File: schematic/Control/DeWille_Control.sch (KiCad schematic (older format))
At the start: 8 parts

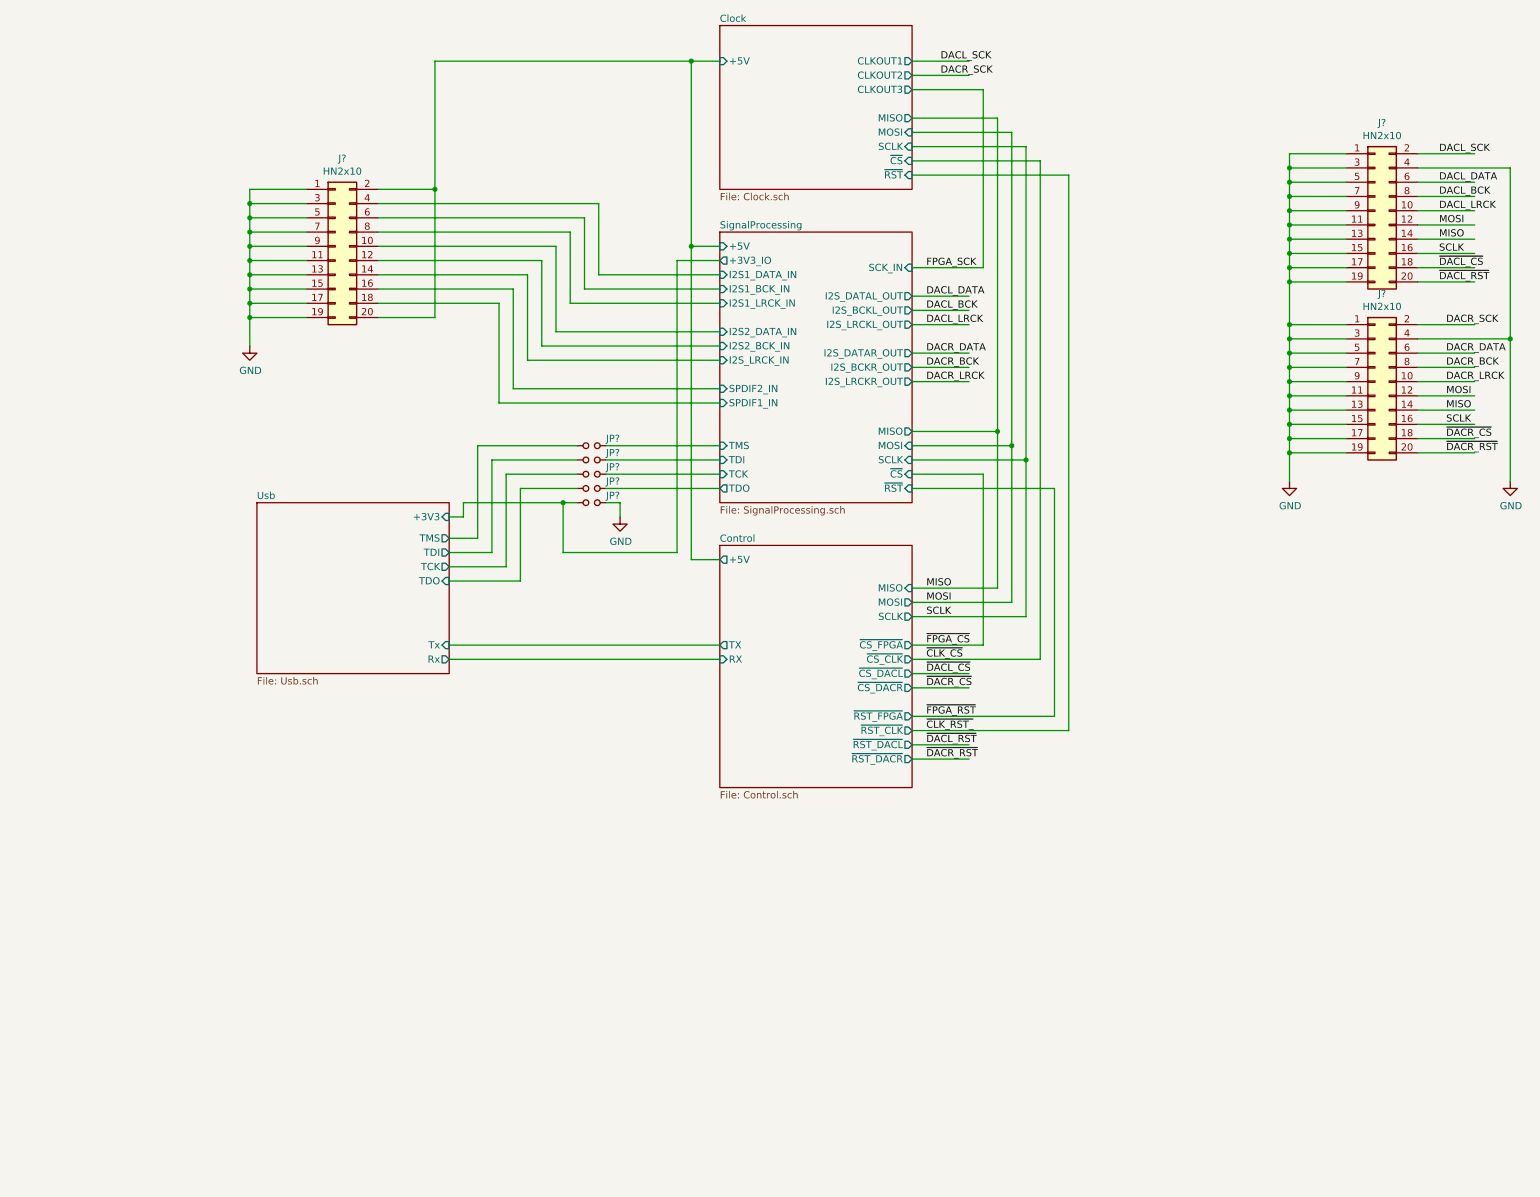
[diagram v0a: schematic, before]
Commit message: Provision for SPI Slave FPGA bitstream download. Switch RAM from x16 to x8 one.
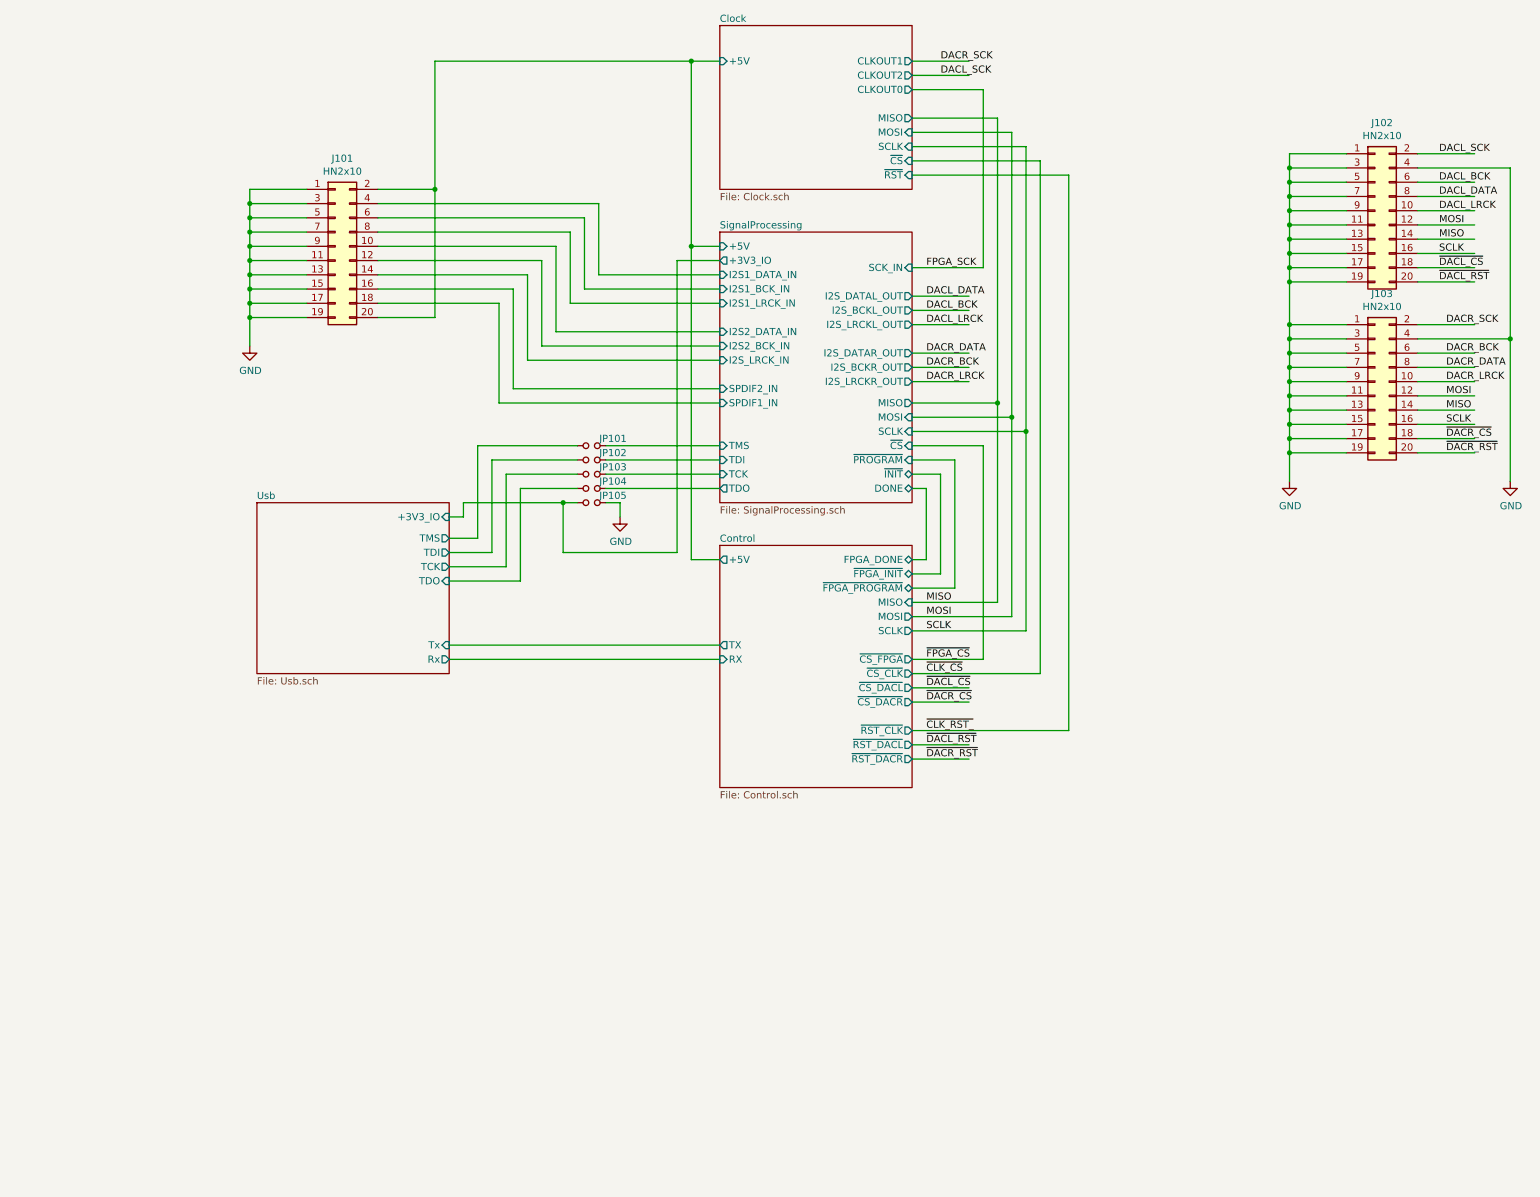
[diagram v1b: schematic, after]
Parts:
- JP101, JP102, JP103, JP104, JP105: renamed from JP?; footprint (none) -> Connector_PinHeader_2.54mm:PinHeader_1x02_P2.54mm_Vertical
- gave numbers to parts that had none: 3
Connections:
- net labels removed: ~FPGA_RST~
- wire segments 186 -> 192

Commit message: Interim commit
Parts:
- added D101: Green, LED_SMD:LED_0805_2012Metric, symbol Device:LED
- added D102, D103, D104, D105: Red, LED_SMD:LED_0805_2012Metric, symbol Device:LED
- added H101, H102, H103, H104: MountingHole, MountingHole:MountingHole_3.2mm_M3_Pad, symbol Mechanical:MountingHole
- added R101, R102, R103, R104, R105: 470, Resistor_SMD:R_0603_1608Metric, symbol Device:R
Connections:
- net labels added: RX, TX
- wire segments 192 -> 225

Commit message: Routing complete
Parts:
- removed JP105: (no value), Connector_PinHeader_2.54mm:PinHeader_1x02_P2.54mm_Vertical, symbol Device:Jumper_NO_Small
- added D?: SM6T6V8CA, Diode_SMD:D_SMB, symbol Diode:1.5KExxCA
- added F?: PFMF.050.2, Fuse:Fuse_1812_4532Metric, symbol Device:Polyfuse
- JP101, JP102, JP103, JP104: footprint Connector_PinHeader_2.54mm:PinHeader_1x02_P2.54mm_Vertical -> Jumper:SolderJumper-2_P1.3mm_Bridged_RoundedPad1.0x1.5mm
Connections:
- wire segments 225 -> 227
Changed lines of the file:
@@
 F18 "LED1" O L 6000 7200 50
 F19 "LED2" O L 6000 7300 50
+F20 "~RST_FPGA~" O R 7350 7400 50
 $EndSheet
 Wire Wire Line
@@
 F4 "MISO" O R 7350 4700 50
 F5 "SCLK" I R 7350 4900 50
-F6 "~CS~" I R 7350 5100 50
+F6 "~FPGA_CS~" I R 7350 5100 50
 F7 "I2S_LRCKL_OUT" O R 7350 4200 50
 F8 "I2S_BCKL_OUT" O R 7350 4100 50
@@
 F17 "I2S2_BCK_IN" I L 6000 4400 50
 F18 "I2S2_LRCK_IN" I L 6000 4500 50
-F19 "SPDIF1_IN" I L 6000 4800 50
-F20 "SPDIF2_IN" I L 6000 4700 50
+F19 "SPDIF1_IN" I L 6000 4700 50
+F20 "SPDIF2_IN" I L 6000 4800 50
 F21 "+5V" I L 6000 3700 50
 F22 "TMS" I L 6000 5100 50
@@
 F 0 "JP101" H 5250 5150 50  0000 C CNN
 F 1 " " H 5100 5194 50  0000 C CNN
-F 2 "Connector_PinHeader_2.54mm:PinHeader_1x02_P2.54mm_Vertical" H 5100 5100 50  0001 C CNN
+F 2 "Jumper:SolderJumper-2_P1.3mm_Bridged_RoundedPad1.0x1.5mm" H 5100 5100 50  0001 C CNN
 F 3 "~" H 5100 5100 50  0001 C CNN
 	1    5100 5100
@@
 F 0 "JP102" H 5250 5250 50  0000 C CNN
 F 1 " " H 5100 5294 50  0000 C CNN
-F 2 "Connector_PinHeader_2.54mm:PinHeader_1x02_P2.54mm_Vertical" H 5100 5200 50  0001 C CNN
+F 2 "Jumper:SolderJumper-2_P1.3mm_Bridged_RoundedPad1.0x1.5mm" H 5100 5200 50  0001 C CNN
 F 3 "~" H 5100 5200 50  0001 C CNN
 	1    5100 5200
@@
 F 0 "JP103" H 5250 5350 50  0000 C CNN
 F 1 " " H 5100 5394 50  0000 C CNN
-F 2 "Connector_PinHeader_2.54mm:PinHeader_1x02_P2.54mm_Vertical" H 5100 5300 50  0001 C CNN
+F 2 "Jumper:SolderJumper-2_P1.3mm_Bridged_RoundedPad1.0x1.5mm" H 5100 5300 50  0001 C CNN
 F 3 "~" H 5100 5300 50  0001 C CNN
 	1    5100 5300
@@
 F 0 "JP104" H 5250 5450 50  0000 C CNN
 F 1 " " H 5100 5494 50  0000 C CNN
-F 2 "Connector_PinHeader_2.54mm:PinHeader_1x02_P2.54mm_Vertical" H 5100 5400 50  0001 C CNN
+F 2 "Jumper:SolderJumper-2_P1.3mm_Bridged_RoundedPad1.0x1.5mm" H 5100 5400 50  0001 C CNN
 F 3 "~" H 5100 5400 50  0001 C CNN
 	1    5100 5400
@@
 Wire Wire Line
 	4600 6050 4100 6050
-$Comp
-L Device:Jumper_NO_Small JP105
-U 1 1 5E2A0271
-P 5100 5500
-F 0 "JP105" H 5250 5550 50  0000 C CNN
-F 1 " " H 5100 5594 50  0000 C CNN
-F 2 "Connector_PinHeader_2.54mm:PinHeader_1x02_P2.54mm_Vertical" H 5100 5500 50  0001 C CNN
-F 3 "~" H 5100 5500 50  0001 C CNN
-	1    5100 5500
-	1    0    0    -1
-$EndComp
 Wire Wire Line
 	4100 5600 4200 5600
@@
 Wire Wire Line
 	4200 5500 4800 5500
-$Comp
-L power:GND #PWR?
-U 1 1 5E2A6414
-P 5300 5600
-AR Path="/5DD2C0D9/5E2A6414" Ref="#PWR?"  Part="1"
-AR Path="/5E2A6414" Ref="#PWR0102"  Part="1"
-F 0 "#PWR0102" H 5300 5350 50  0001 C CNN
-F 1 "GND" H 5305 5427 50  0000 C CNN
-F 2 "" H 5300 5600 50  0001 C CNN
-F 3 "" H 5300 5600 50  0001 C CNN
-	1    5300 5600
-	1    0    0    -1
-$EndComp
-Wire Wire Line
-	5200 5500 5300 5500
-Wire Wire Line
-	5300 5500 5300 5600
 Wire Wire Line
 	3100 4100 2700 4100
@@
 Wire Wire Line
 	4800 5900 4800 5500
-Connection ~ 4800 5500
-Wire Wire Line
-	4800 5500 5000 5500
 Wire Wire Line
 	8250 3100 8250 6700
@@
 	2900 2400 2900 3300
 Wire Wire Line
-	2900 2400 5800 2400
+	2900 2400 3300 2400
 Connection ~ 2900 3300
 Wire Wire Line
@@
 Wire Wire Line
 	5250 3900 6000 3900
+Wire Wire Line
+	7350 7400 8350 7400
+Wire Wire Line
+	8350 7400 8350 5000
+Wire Wire Line
+	8350 5000 7350 5000
+$Comp
+L Device:Polyfuse F?
+U 1 1 5E641952
+P 3450 2400
+F 0 "F?" V 3225 2400 50  0000 C CNN
+F 1 "PFMF.050.2" V 3316 2400 50  0000 C CNN
+F 2 "Fuse:Fuse_1812_4532Metric" H 3500 2200 50  0001 L CNN
+F 3 "~" H 3450 2400 50  0001 C CNN
+	1    3450 2400
+	0    1    1    0
+$EndComp
+$Comp
+L power:GND #PWR?
+U 1 1 5E644AF9
+P 3850 2700
+AR Path="/5DD2C0D9/5E644AF9" Ref="#PWR?"  Part="1"
+AR Path="/5E644AF9" Ref="#PWR?"  Part="1"
+F 0 "#PWR?" H 3850 2450 50  0001 C CNN
+F 1 "GND" H 3855 2527 50  0000 C CNN
+F 2 "" H 3850 2700 50  0001 C CNN
+F 3 "" H 3850 2700 50  0001 C CNN
+	1    3850 2700
+	1    0    0    -1
+$EndComp
+Wire Wire Line
+	3600 2400 3850 2400
+$Comp
+L Diode:1.5KExxCA D?
+U 1 1 5E656D9F
+P 3850 2550
+F 0 "D?" V 3804 2629 50  0000 L CNN
+F 1 "SM6T6V8CA" V 3895 2629 50  0000 L CNN
+F 2 "Diode_SMD:D_SMB" H 3850 2350 50  0001 C CNN
+F 3 "https://www.vishay.com/docs/88301/15ke.pdf" H 3850 2550 50  0001 C CNN
+	1    3850 2550
+	0    1    1    0
+$EndComp
+Connection ~ 3850 2400
+Wire Wire Line
+	3850 2400 5800 2400
 $EndSCHEMATC

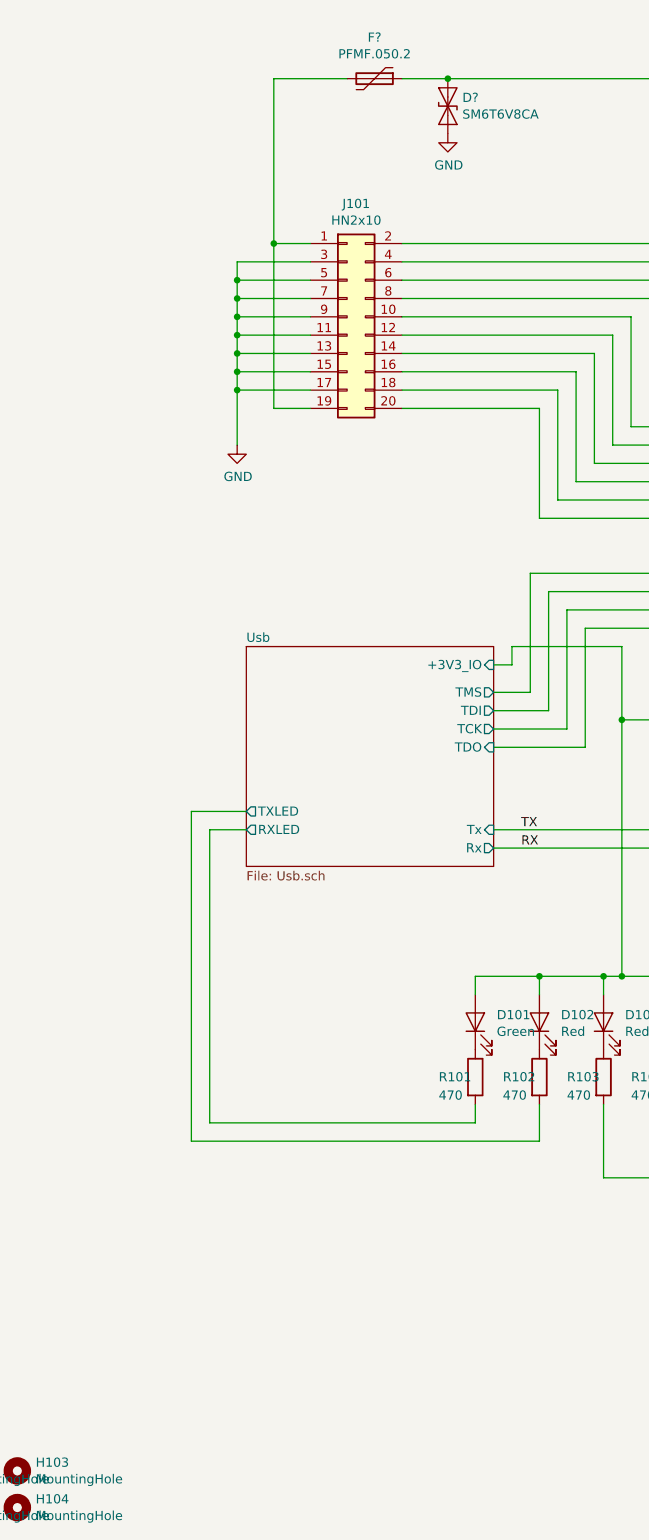
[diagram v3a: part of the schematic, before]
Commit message: Add source termination resistors to I2S output lines. Arrange top silk information.
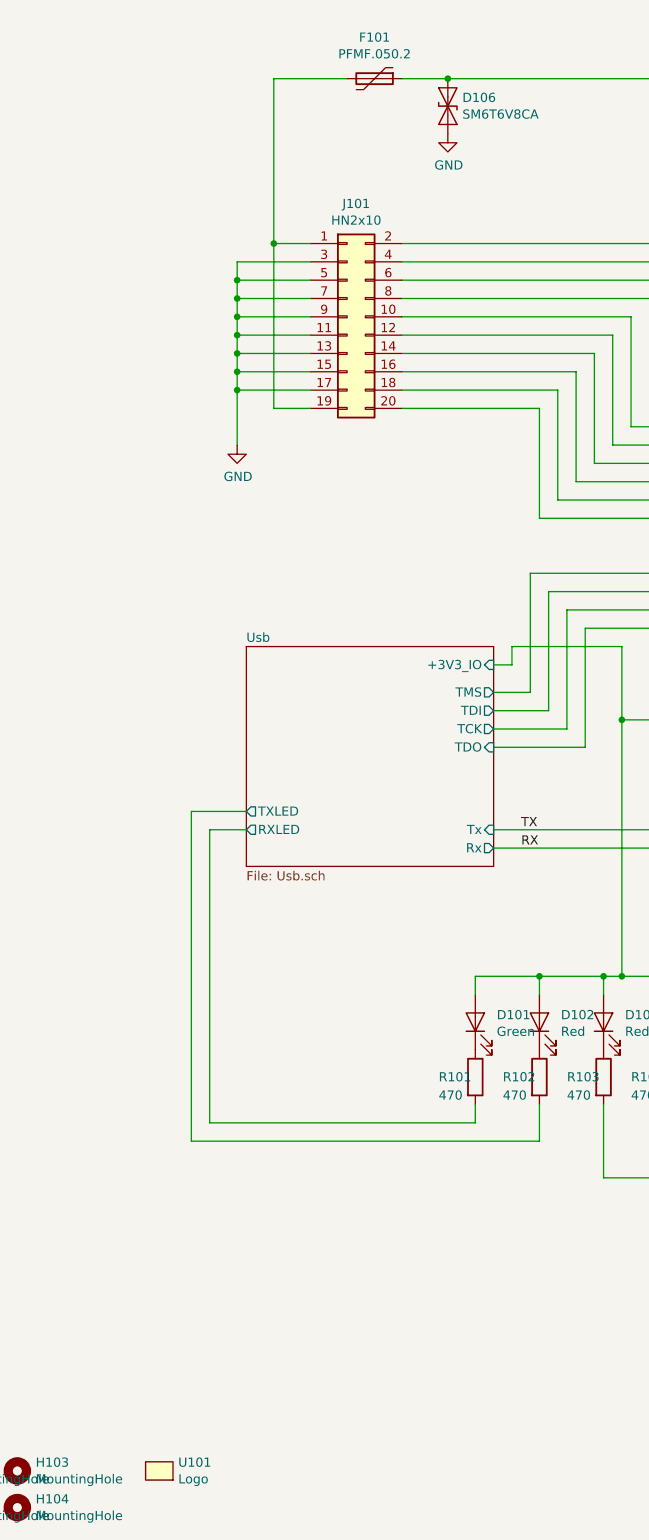
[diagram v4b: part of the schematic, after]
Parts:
- added U101: Logo, Zmei_Footprints:Zmei-logo-small-inverted_nosilk, symbol Zmei_elements:Logo
- gave numbers to parts that had none: 2
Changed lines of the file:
@@
 	8350 5000 7350 5000
 $Comp
-L Device:Polyfuse F?
+L Device:Polyfuse F101
 U 1 1 5E641952
 P 3450 2400
-F 0 "F?" V 3225 2400 50  0000 C CNN
+F 0 "F101" V 3225 2400 50  0000 C CNN
 F 1 "PFMF.050.2" V 3316 2400 50  0000 C CNN
 F 2 "Fuse:Fuse_1812_4532Metric" H 3500 2200 50  0001 L CNN
@@
 P 3850 2700
 AR Path="/5DD2C0D9/5E644AF9" Ref="#PWR?"  Part="1"
-AR Path="/5E644AF9" Ref="#PWR?"  Part="1"
-F 0 "#PWR?" H 3850 2450 50  0001 C CNN
+AR Path="/5E644AF9" Ref="#PWR0149"  Part="1"
+F 0 "#PWR0149" H 3850 2450 50  0001 C CNN
 F 1 "GND" H 3855 2527 50  0000 C CNN
 F 2 "" H 3850 2700 50  0001 C CNN
@@
 	3600 2400 3850 2400
 $Comp
-L Diode:1.5KExxCA D?
+L Diode:1.5KExxCA D106
 U 1 1 5E656D9F
 P 3850 2550
-F 0 "D?" V 3804 2629 50  0000 L CNN
+F 0 "D106" V 3804 2629 50  0000 L CNN
 F 1 "SM6T6V8CA" V 3895 2629 50  0000 L CNN
 F 2 "Diode_SMD:D_SMB" H 3850 2350 50  0001 C CNN
@@
 Wire Wire Line
 	3850 2400 5800 2400
+$Comp
+L Zmei_elements:Logo U101
+U 1 1 5E70F649
+P 2300 9850
+F 0 "U101" H 2378 9746 50  0000 L CNN
+F 1 "Logo" H 2378 9655 50  0000 L CNN
+F 2 "Zmei_Footprints:Zmei-logo-small-inverted_nosilk" H 2300 9850 50  0001 C CNN
+F 3 "" H 2300 9850 50  0001 C CNN
+	1    2300 9850
+	1    0    0    -1
+$EndComp
 $EndSCHEMATC
